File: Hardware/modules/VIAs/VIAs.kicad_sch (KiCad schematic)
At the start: 9 parts, among them J1 Bus_PCI_6502, J2 Port 1, J3 Port 2, U1 W65C22SxP, U2 W65C22SxP, U3 74HC138

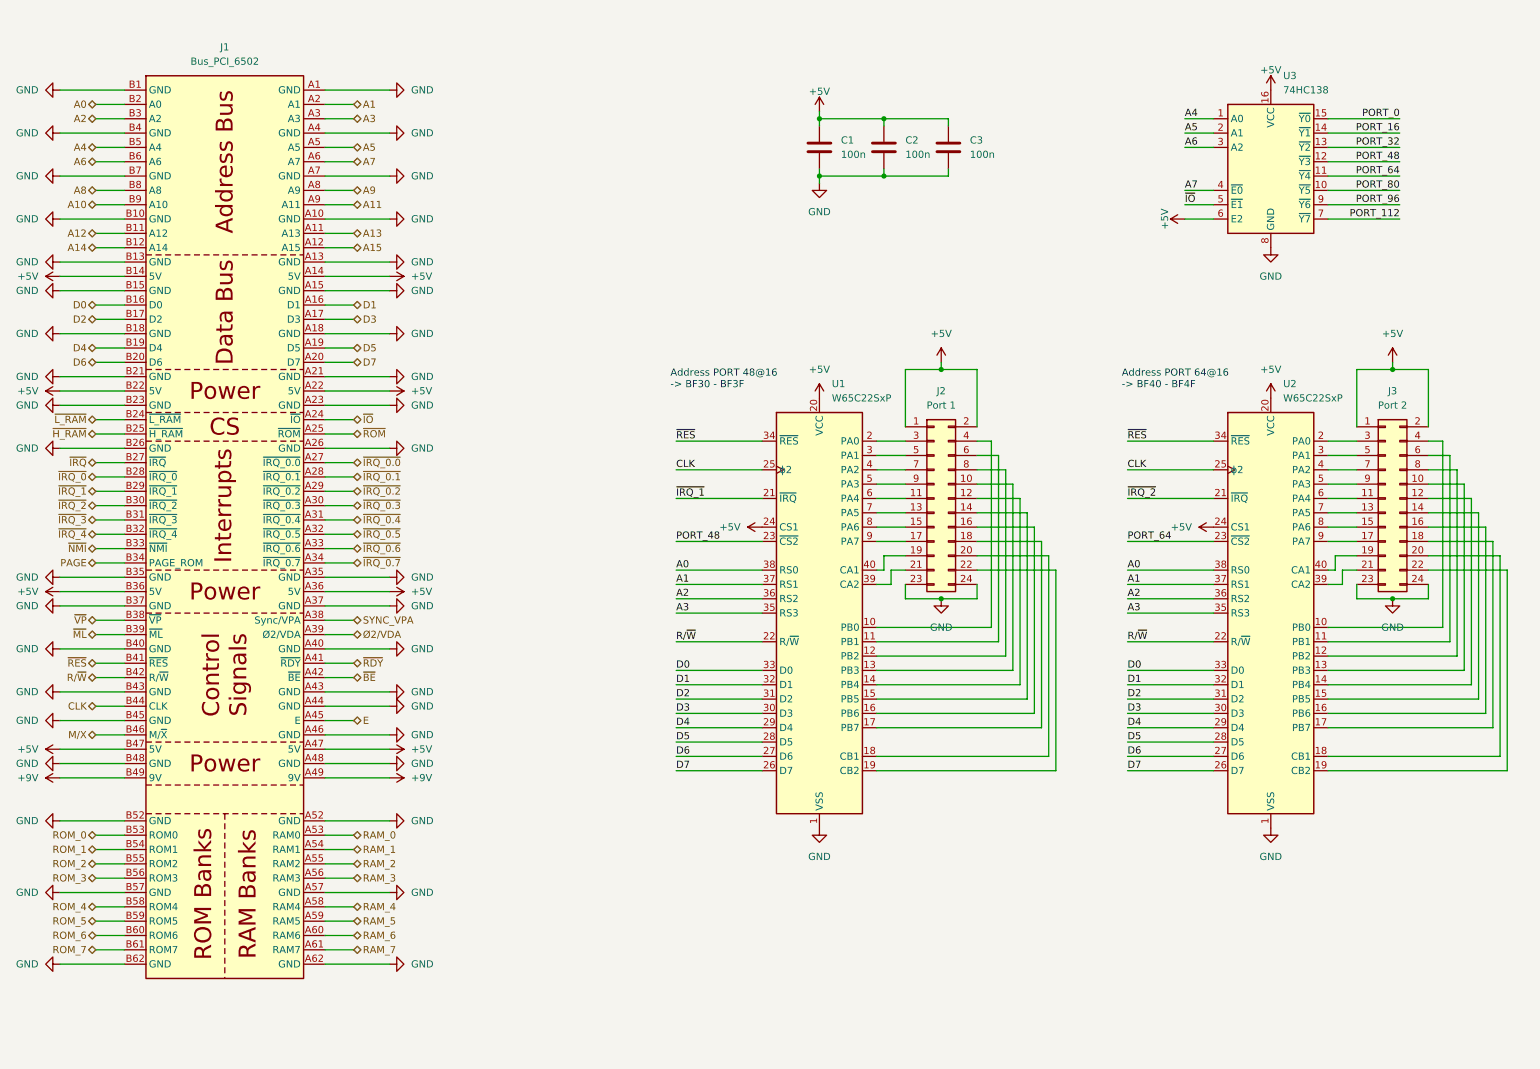
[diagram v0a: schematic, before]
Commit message: Hardware Update Add MyCPU VGA Module Beautify all Schematics minor Error corrections Readme Update
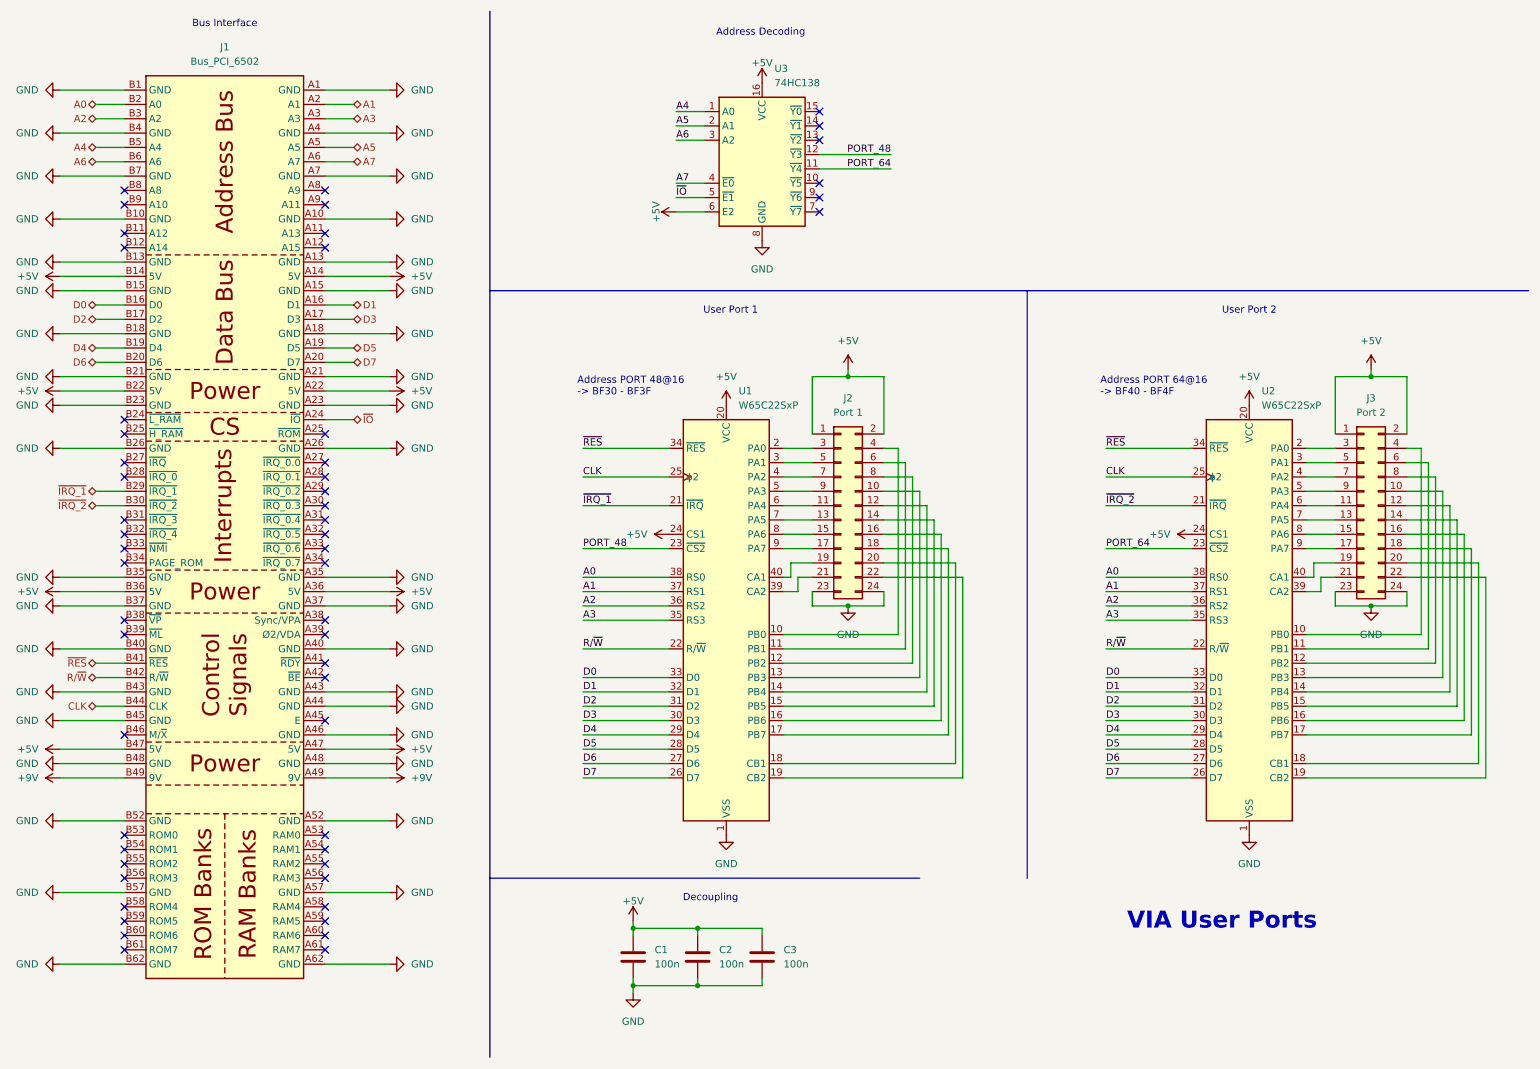
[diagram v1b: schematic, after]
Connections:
- net A10: no longer names the net of J1.B9 (A10)
- net A11: no longer names the net of J1.A9 (A11)
- net A12: no longer names the net of J1.B11 (A12)
- net A13: no longer names the net of J1.A11 (A13)
- net A14: no longer names the net of J1.B12 (A14)
- net A15: no longer names the net of J1.A12 (A15)
- net A8: no longer names the net of J1.B8 (A8)
- net A9: no longer names the net of J1.A8 (A9)
- net E: no longer names the net of J1.A45 (E)
- net M/X: no longer names the net of J1.B46 (M/~{X})
- net PAGE: no longer names the net of J1.B34 (PAGE_ROM)
- net PORT_0: no longer names the net of U3.15 (~{Y0})
- net PORT_112: no longer names the net of U3.7 (~{Y7})
- net PORT_16: no longer names the net of U3.14 (~{Y1})
- net PORT_32: no longer names the net of U3.13 (~{Y2})
- net PORT_80: no longer names the net of U3.10 (~{Y5})
- net PORT_96: no longer names the net of U3.9 (~{Y6})
- net RAM_0: no longer names the net of J1.A53 (RAM0)
- net RAM_1: no longer names the net of J1.A54 (RAM1)
- net RAM_2: no longer names the net of J1.A55 (RAM2)
- net RAM_3: no longer names the net of J1.A56 (RAM3)
- net RAM_4: no longer names the net of J1.A58 (RAM4)
- net RAM_5: no longer names the net of J1.A59 (RAM5)
- net RAM_6: no longer names the net of J1.A60 (RAM6)
- net RAM_7: no longer names the net of J1.A61 (RAM7)
- net ROM_0: no longer names the net of J1.B53 (ROM0)
- net ROM_1: no longer names the net of J1.B54 (ROM1)
- net ROM_2: no longer names the net of J1.B55 (ROM2)
- net ROM_3: no longer names the net of J1.B56 (ROM3)
- net ROM_4: no longer names the net of J1.B58 (ROM4)
- net ROM_5: no longer names the net of J1.B59 (ROM5)
- net ROM_6: no longer names the net of J1.B60 (ROM6)
- net ROM_7: no longer names the net of J1.B61 (ROM7)
- net SYNC_VPA: no longer names the net of J1.A38 (Sync/VPA)
- net ~{BE}: no longer names the net of J1.A42 (~{BE})
- net ~{H_RAM}: no longer names the net of J1.B25 (~{H_RAM})
- net ~{IRQ_0.0}: no longer names the net of J1.A27 (~{IRQ_0.0})
- net ~{IRQ_0.1}: no longer names the net of J1.A28 (~{IRQ_0.1})
- net ~{IRQ_0.2}: no longer names the net of J1.A29 (~{IRQ_0.2})
- net ~{IRQ_0.3}: no longer names the net of J1.A30 (~{IRQ_0.3})
- net ~{IRQ_0.4}: no longer names the net of J1.A31 (~{IRQ_0.4})
- net ~{IRQ_0.5}: no longer names the net of J1.A32 (~{IRQ_0.5})
- net ~{IRQ_0.6}: no longer names the net of J1.A33 (~{IRQ_0.6})
- net ~{IRQ_0.7}: no longer names the net of J1.A34 (~{IRQ_0.7})
- net ~{IRQ_0}: no longer names the net of J1.B28 (~{IRQ_0})
- net ~{IRQ_3}: no longer names the net of J1.B31 (~{IRQ_3})
- net ~{IRQ_4}: no longer names the net of J1.B32 (~{IRQ_4})
- net ~{IRQ}: no longer names the net of J1.B27 (~{IRQ})
- net ~{L_RAM}: no longer names the net of J1.B24 (~{L_RAM})
- net ~{ML}: no longer names the net of J1.B39 (~{ML})
- net ~{NMI}: no longer names the net of J1.B33 (~{NMI})
- net ~{RDY}: no longer names the net of J1.A41 (~{RDY})
- net ~{ROM}: no longer names the net of J1.A25 (~{ROM})
- net ~{VP}: no longer names the net of J1.B38 (~{VP})
- net Ø2/VDA: no longer names the net of J1.A39 (Ø2/VDA)
- no-connect marks 0 -> 55
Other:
- note added: "Address Decoding"
- note added: "Bus Interface"
- note added: "Decoupling"
- note added: "User Port 1"
- note added: "User Port 2"
- note added: "VIA User Ports"
- company: (none) -> Synthron
- title: (none) -> S65xx Computer System
- moved on the sheet: C1, C2, C3, J2, J3, U1, U2, U3

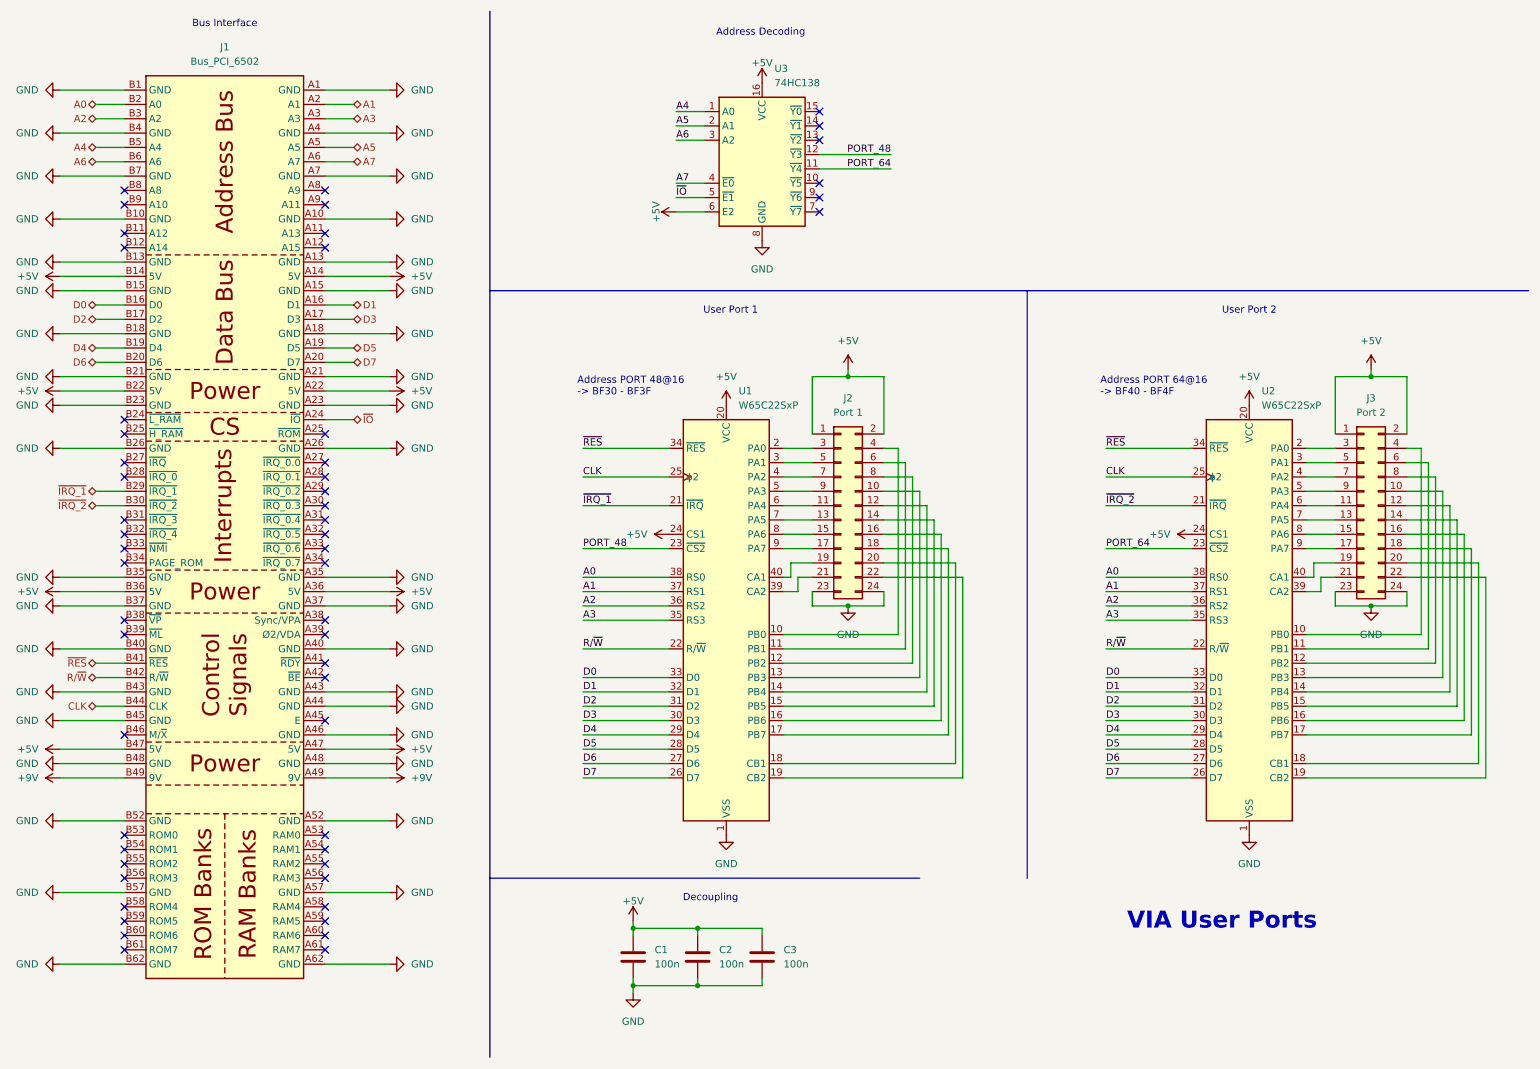
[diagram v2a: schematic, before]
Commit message: Hardware Review Pt. 1 fix Address Decoding for Strobe Generators add bulk capacitance to every board fix wiring of Prototyping Board
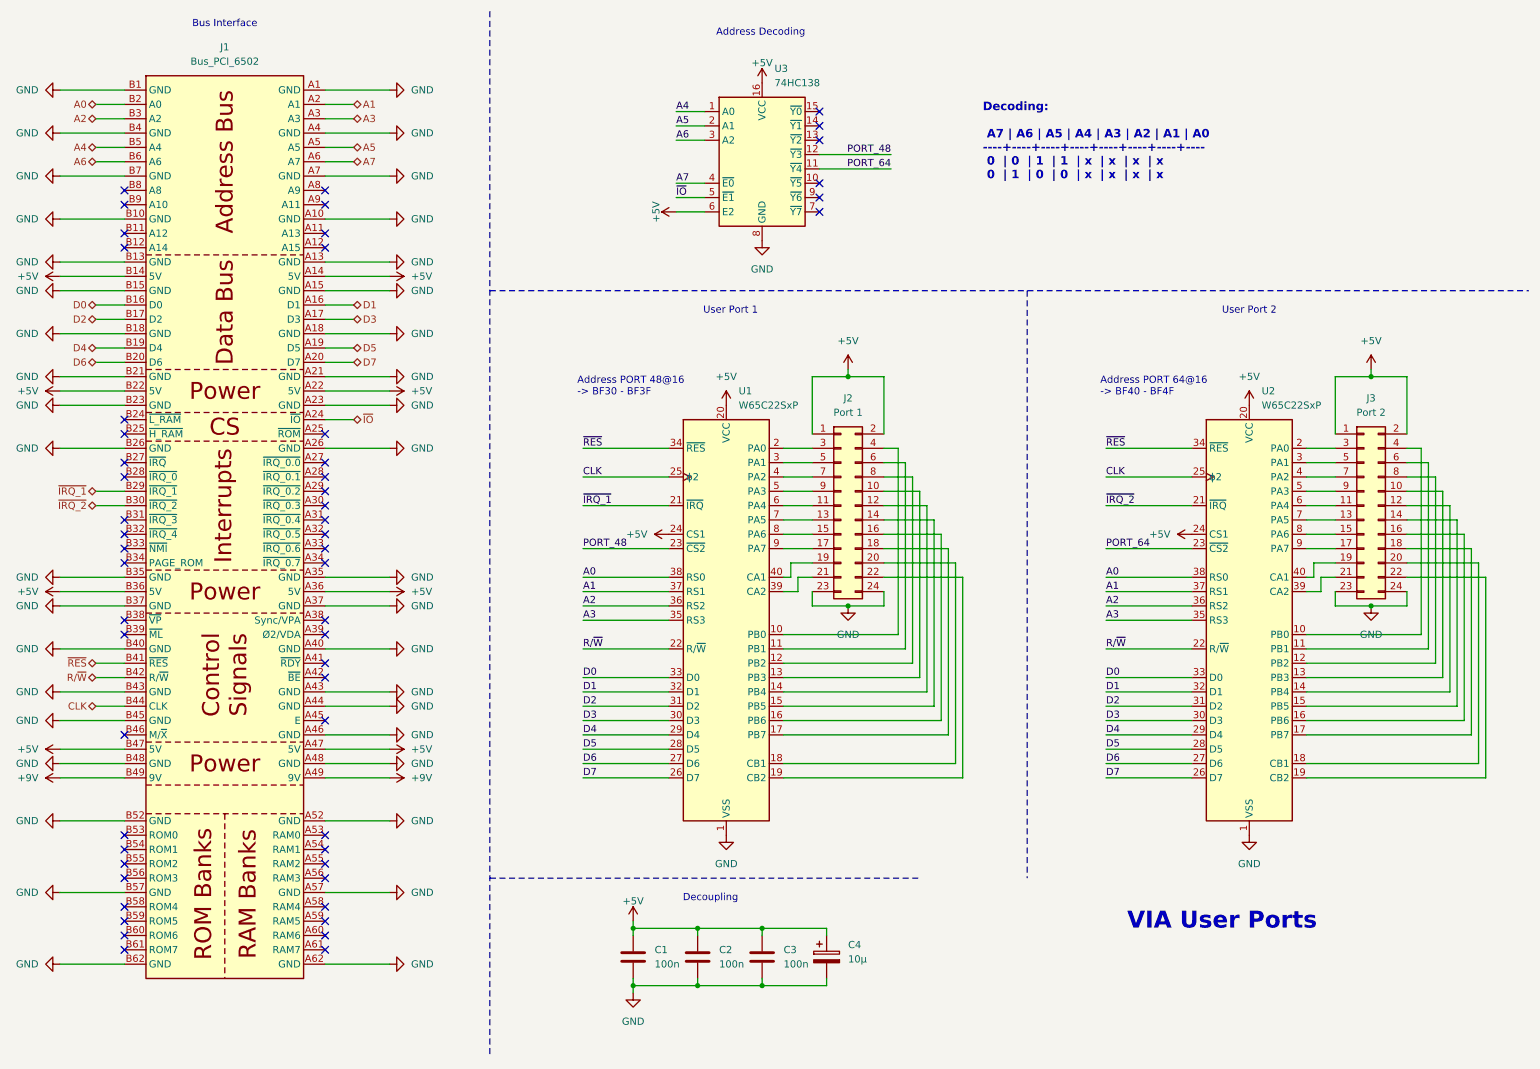
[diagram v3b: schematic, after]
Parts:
- added C4: 10µ, Capacitor_THT:CP_Radial_D5.0mm_P2.50mm, symbol Device:C_Polarized
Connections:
- net +5V: now also C4.1
- net GND: now also C4.2
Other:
- note added: "Decoding: A7 | A6 | A5 | A4 | A3 | A2 | A1 | A0 ----+----+----+----+----+----+----+---- 0 | 0 | 1 | 1 | x | x | x | x 0 | 1 | 0 | 0 | x | x | x | x"
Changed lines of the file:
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@@
 	)
 	(junction
+		(at 148.59 175.26)
+		(diameter 0)
+		(color 0 0 0 0)
+	)
+	(junction
 		(at 125.73 185.42)
 		(diameter 0)
@@
 	)
 	(junction
+		(at 148.59 185.42)
+		(diameter 0)
+		(color 0 0 0 0)
+	)
+	(junction
 		(at 256.54 118.11)
 		(diameter 0)
@@
 	(wire
 		(pts
+			(xy 160.02 176.53) (xy 160.02 175.26)
+		)
+		(stroke
+			(width 0)
+			(type default)
+		)
+	)
+	(wire
+		(pts
 			(xy 82.55 34.29) (xy 71.12 34.29)
 		)
@@
 		(stroke
 			(width 0)
-			(type default)
+			(type dash)
 		)
 	)
@@
 		(stroke
 			(width 0)
-			(type default)
+			(type dash)
 		)
 	)
@@
 	(wire
 		(pts
+			(xy 160.02 184.15) (xy 160.02 185.42)
+		)
+		(stroke
+			(width 0)
+			(type default)
+		)
+	)
+	(wire
+		(pts
 			(xy 30.48 130.81) (xy 35.56 130.81)
 		)
@@
 	(wire
 		(pts
+			(xy 160.02 175.26) (xy 148.59 175.26)
+		)
+		(stroke
+			(width 0)
+			(type default)
+		)
+	)
+	(wire
+		(pts
 			(xy 265.43 123.19) (xy 265.43 90.17)
 		)
@@
 		(stroke
 			(width 0)
-			(type default)
+			(type dash)
 		)
 	)
@@
 		(stroke
 			(width 0)
-			(type default)
+			(type dash)
 		)
 	)
@@
 	(wire
 		(pts
+			(xy 160.02 185.42) (xy 148.59 185.42)
+		)
+		(stroke
+			(width 0)
+			(type default)
+		)
+	)
+	(wire
+		(pts
 			(xy 137.16 185.42) (xy 125.73 185.42)
 		)
@@
 		)
 	)
+	(text "Decoding:\n\n A7 | A6 | A5 | A4 | A3 | A2 | A1 | A0\n----+----+----+----+----+----+----+----\n 0  | 0  | 1  | 1  | x  | x  | x  | x\n 0  | 1  | 0  | 0  | x  | x  | x  | x"
+		(exclude_from_sim no)
+		(at 187.706 35.814 0)
+		(effects
+			(font
+				(face "DejaVu Sans Mono")
+				(size 1.5 1.5)
+				(thickness 0.254)
+				(bold yes)
+			)
+			(justify left)
+		)
+	)
 	(text "User Port 1"
 		(exclude_from_sim no)
@@
 	)
 	(symbol
+		(lib_id "Device:C_Polarized")
+		(at 160.02 180.34 0)
+		(unit 1)
+		(exclude_from_sim no)
+		(in_bom yes)
+		(on_board yes)
+		(dnp no)
+		(fields_autoplaced yes)
+		(property "Reference" "C4"
+			(at 163.83 178.1809 0)
+			(effects
+				(font
+					(size 1.27 1.27)
+				)
+				(justify left)
+			)
+		)
+		(property "Value" "10µ"
+			(at 163.83 180.7209 0)
+			(effects
+				(font
+					(size 1.27 1.27)
+				)
+				(justify left)
+			)
+		)
+		(property "Footprint" "Capacitor_THT:CP_Radial_D5.0mm_P2.50mm"
+			(at 160.9852 184.15 0)
+			(effects
+				(font
+					(size 1.27 1.27)
+				)
+				(hide yes)
+			)
+		)
+		(property "Datasheet" "~"
+			(at 160.02 180.34 0)
+			(effects
+				(font
+					(size 1.27 1.27)
+				)
+				(hide yes)
+			)
+		)
+		(property "Description" "Polarized capacitor"
+			(at 160.02 180.34 0)
+			(effects
+				(font
+					(size 1.27 1.27)
+				)
+				(hide yes)
+			)
+		)
+		(pin "1"
+		)
+		(pin "2"
+		)
+		(instances
+			(project "VIAs"
+				(path "/35f827ca-0f79-4eb4-a257-c06c3e85a2dd"
+					(reference "C4")
+					(unit 1)
+				)
+			)
+		)
+	)
+	(symbol
 		(lib_id "power:GND")
 		(at 24.13 34.29 270)
@@
 		)
 	)
+	(sheet_instances
+		(path "/"
+			(page "1")
+		)
+	)
